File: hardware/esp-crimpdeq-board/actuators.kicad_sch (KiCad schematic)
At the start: 6 parts, among them SW1 SW_Push, SW2 SW_Push

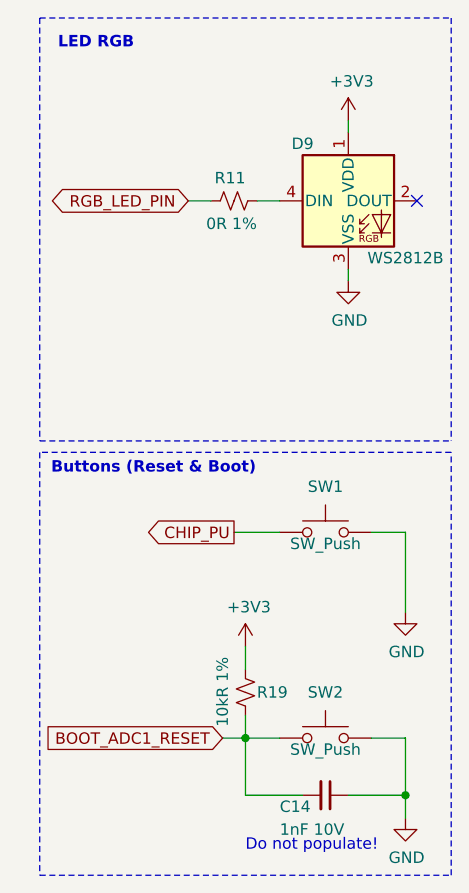
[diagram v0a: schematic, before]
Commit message: Ordering sdchematic in different sheets
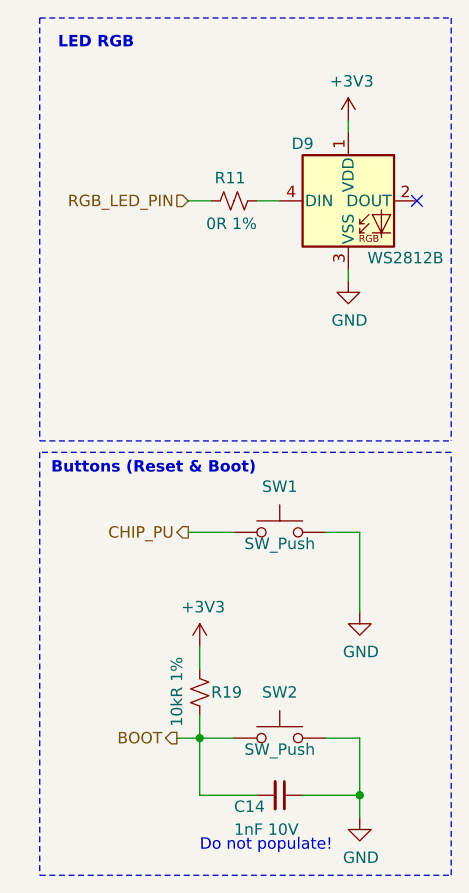
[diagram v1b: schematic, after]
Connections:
- net BOOT_ADC1_RESET renamed BOOT
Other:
- moved on the sheet: C14, R19, SW1, SW2
